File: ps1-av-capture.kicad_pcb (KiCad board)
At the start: 4 copper layers, 100 x 80 mm, 237 parts, among them J1 AV_PIGTAIL, J2 USB3_B, J3 USB_C_AUDIO, J4 JTAG, J5 UART, SW1 RESET, U1 TVP7002PZP, U10 TLV75733PDBVR, U11 TLV75533PDBVR, U12 PCM2903CDBR, U2 CYUSB3014-BZXI, U3 24LC1025-I/SN, U4 24LC1025-I/SN, U5 TPS563201DDCR, U6 TPS563201DDCR, U7 TPS563201DDCR, U8 TLV75519PDBVR, U9 TLV75519PDBVR, X1 27MHz, Y1 19.2MHz, Y2 12MHz

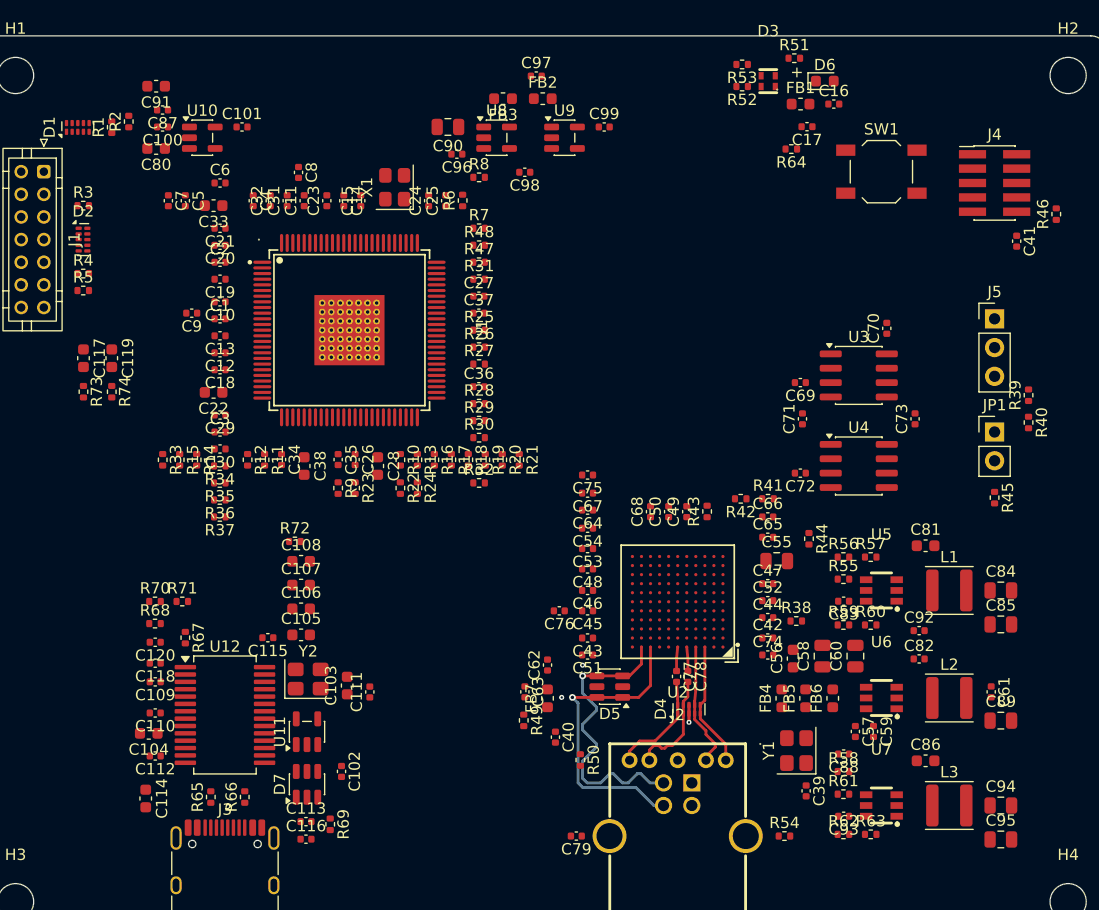
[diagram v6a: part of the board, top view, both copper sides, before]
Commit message: Layout: scripted plane fanout before the autorouter
fanout.py stubs every SMD pad on GND/+3V3/+1V2 to a 0.45 mm via where its plane
covers the spot (FX3 balls dogbone into the diagonal gap, TVP7002 ground pins
strap onto the exposed pad): 238 of 284 pads. +1V2 island cut back to the FX3
and its own buck; plane nets get their own 0.25 mm class.
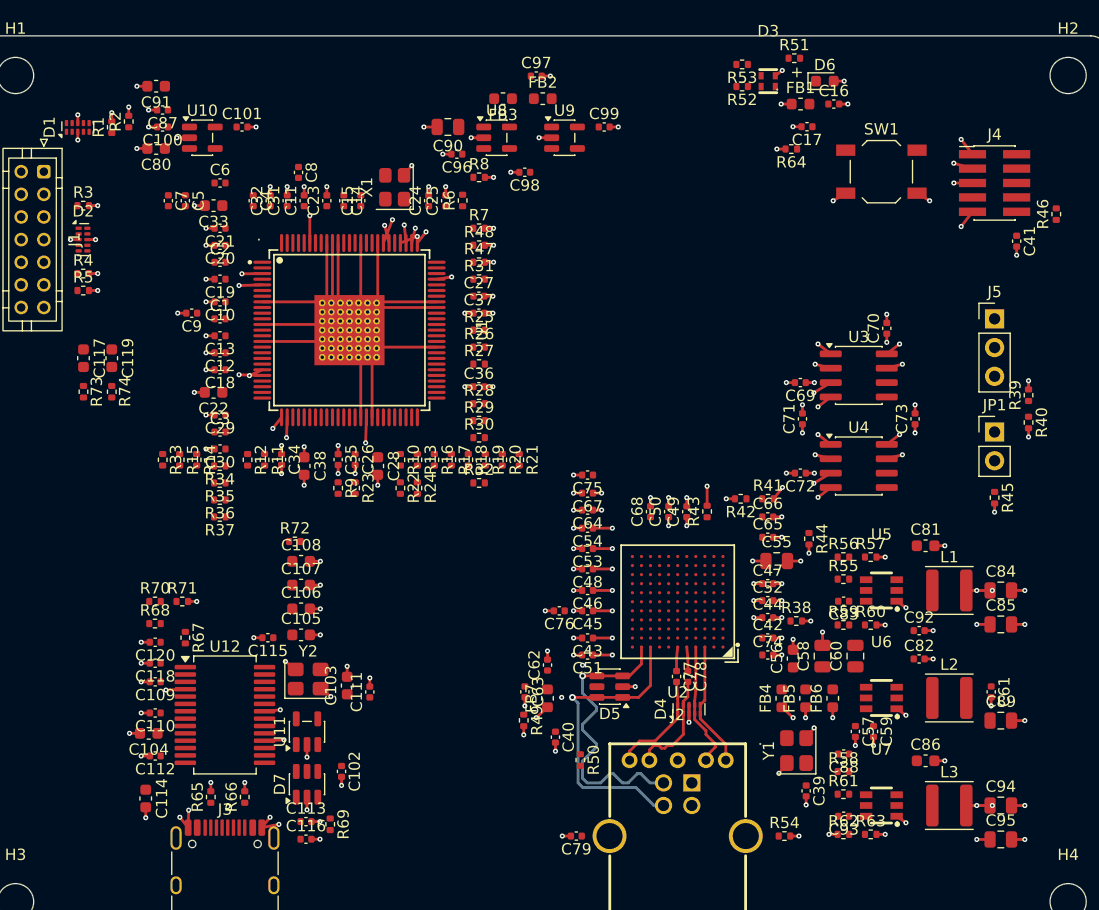
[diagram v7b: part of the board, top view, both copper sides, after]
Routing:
- net GND: track 1.53 -> 231.3 mm, vias 3 -> 175
- net +3V3: track 0.00 -> 36.9 mm, vias 0 -> 33
- net +1V2: track 0.00 -> 25.6 mm, vias 0 -> 20

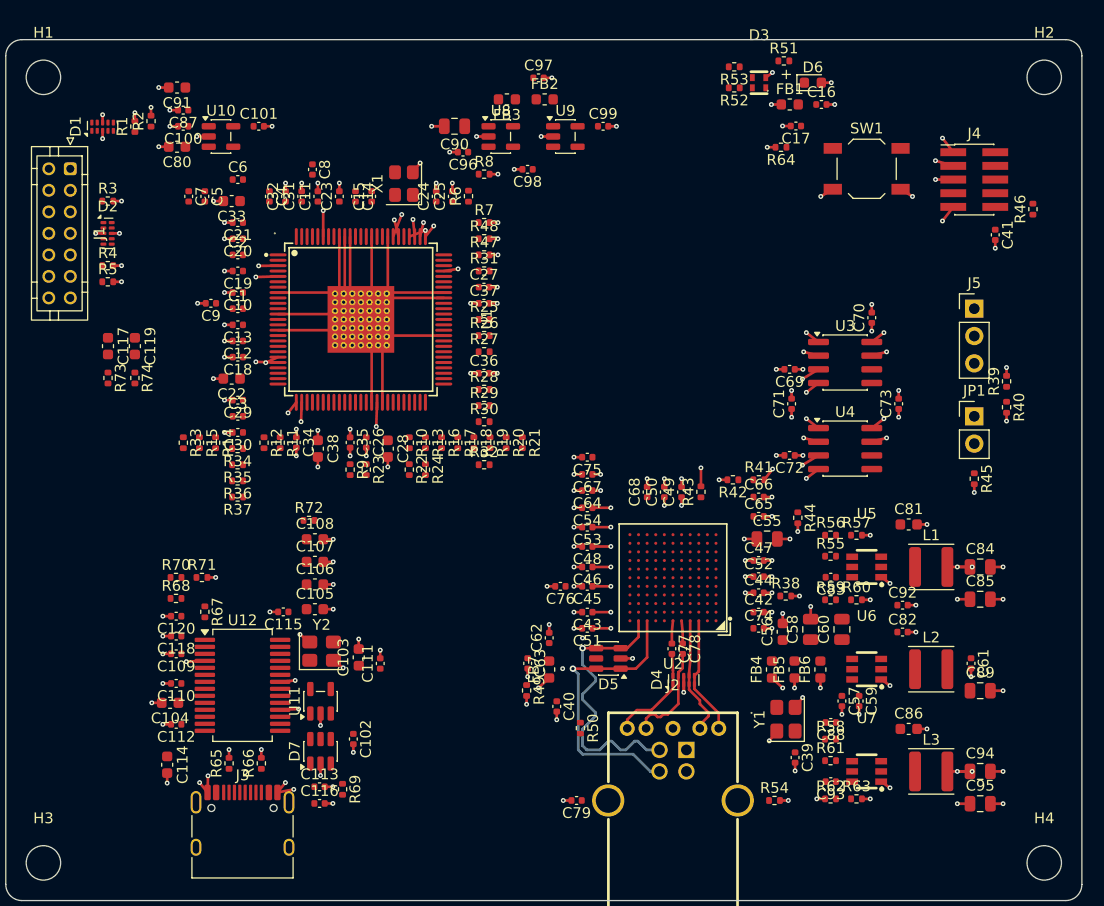
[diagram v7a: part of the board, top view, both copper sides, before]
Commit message: Layout: L3 opened to signals, 0.5 mm placement gap
Freerouting with only L1/L4 for signals stalled at 89 unrouted (16 violations)
after the plane fanout. L3 keeps its supply pours and now also takes signals,
except over the GND island under the USB corridor (rule area: no tracks).
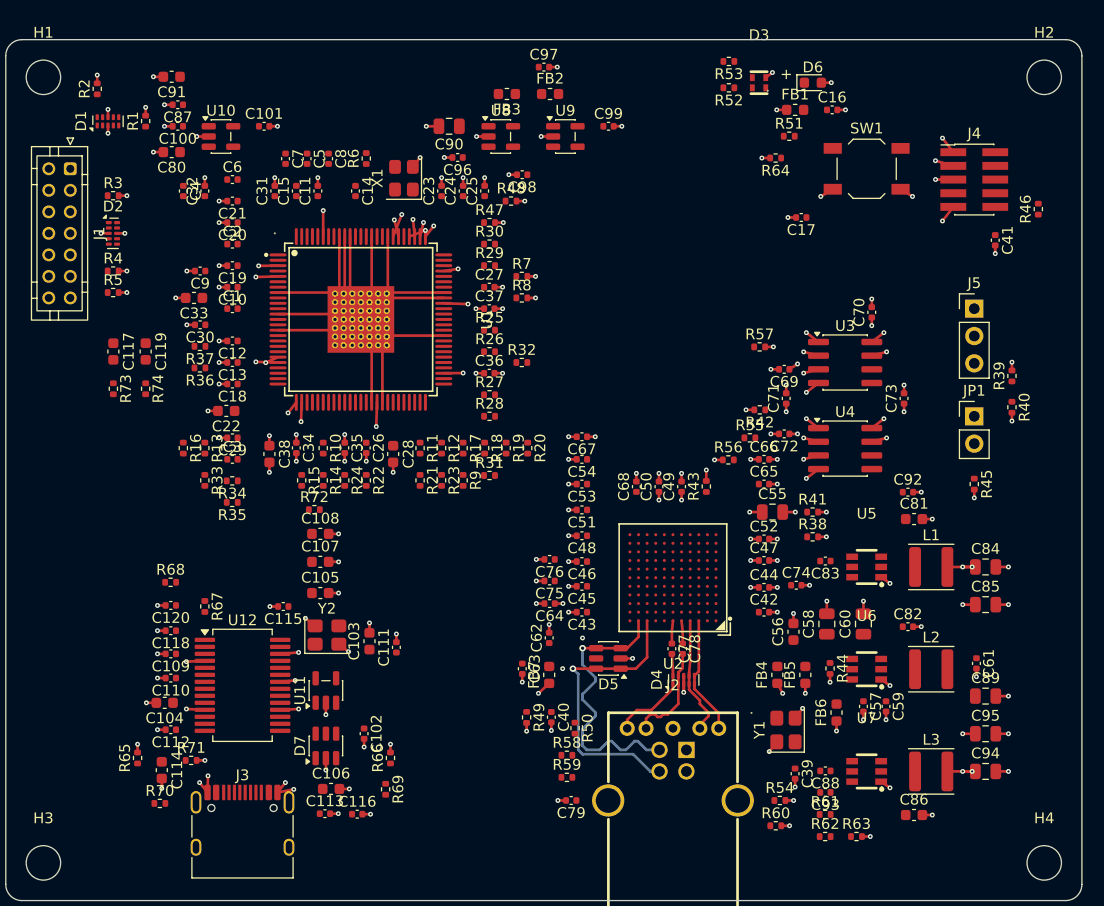
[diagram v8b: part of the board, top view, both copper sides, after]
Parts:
- moved R59 29.5 mm to (152.1, 168.6)
- moved R58 24.5 mm to (152.1, 166.5)
- moved R16 24.0 mm to (116.5, 138.0)
- moved R60 22.3 mm to (171.6, 173.1)
- moved R70 21.1 mm to (114.3, 171.0)
- moved R13 20.5 mm to (118.5, 138.0)
- moved R57 19.7 mm to (170.1, 128.6)
- moved C106 19.1 mm to (130.2, 169.6)
- moved R31 19.0 mm to (145.0, 140.5)
- moved R71 17.0 mm to (117.2, 167.0)
- moved R12 16.5 mm to (140.5, 138.0)
- moved R30 16.5 mm to (145.0, 119.0)
- moved R37 14.4 mm to (118.0, 128.5)
- moved R44 14.3 mm to (176.6, 158.4)
- moved R55 13.3 mm to (169.1, 137.0)
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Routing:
- net +1V2: track 25.6 -> 12.5 mm, vias 20 -> 12
- net GND: track 231.3 -> 235.9 mm, vias 175 -> 178
- net +3V3: track 36.9 -> 40.8 mm, vias 33 -> 37
